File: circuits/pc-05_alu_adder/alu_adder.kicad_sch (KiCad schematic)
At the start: 10 parts, among them J1 Conn_01x10, U1 74LS83, U2 74LS83, U3 74AHC244

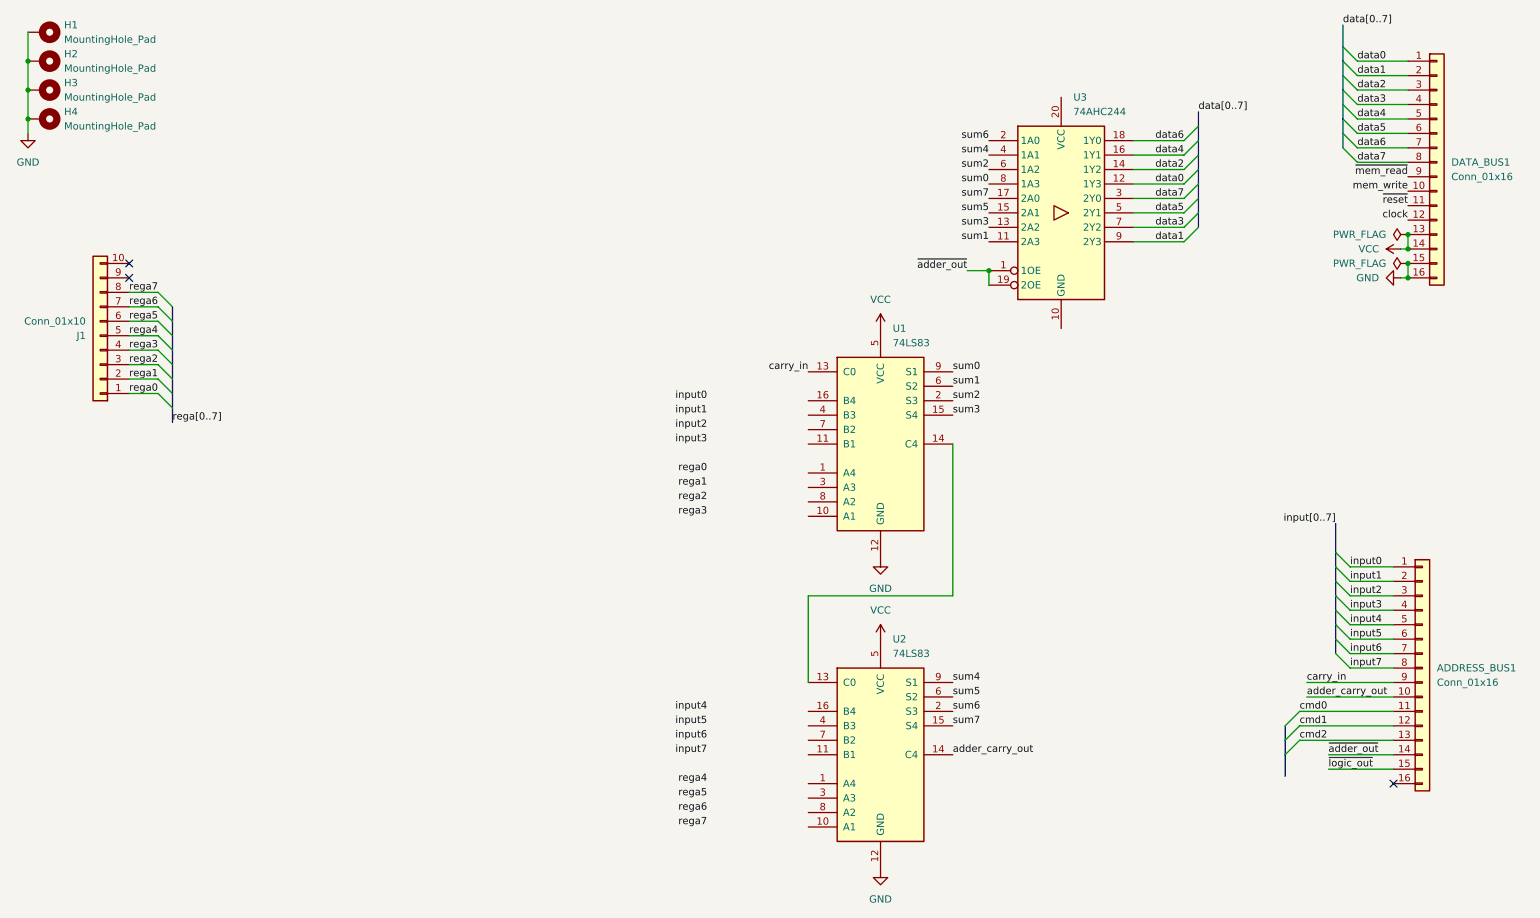
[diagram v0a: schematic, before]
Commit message: pc-05: ALU adder prototype
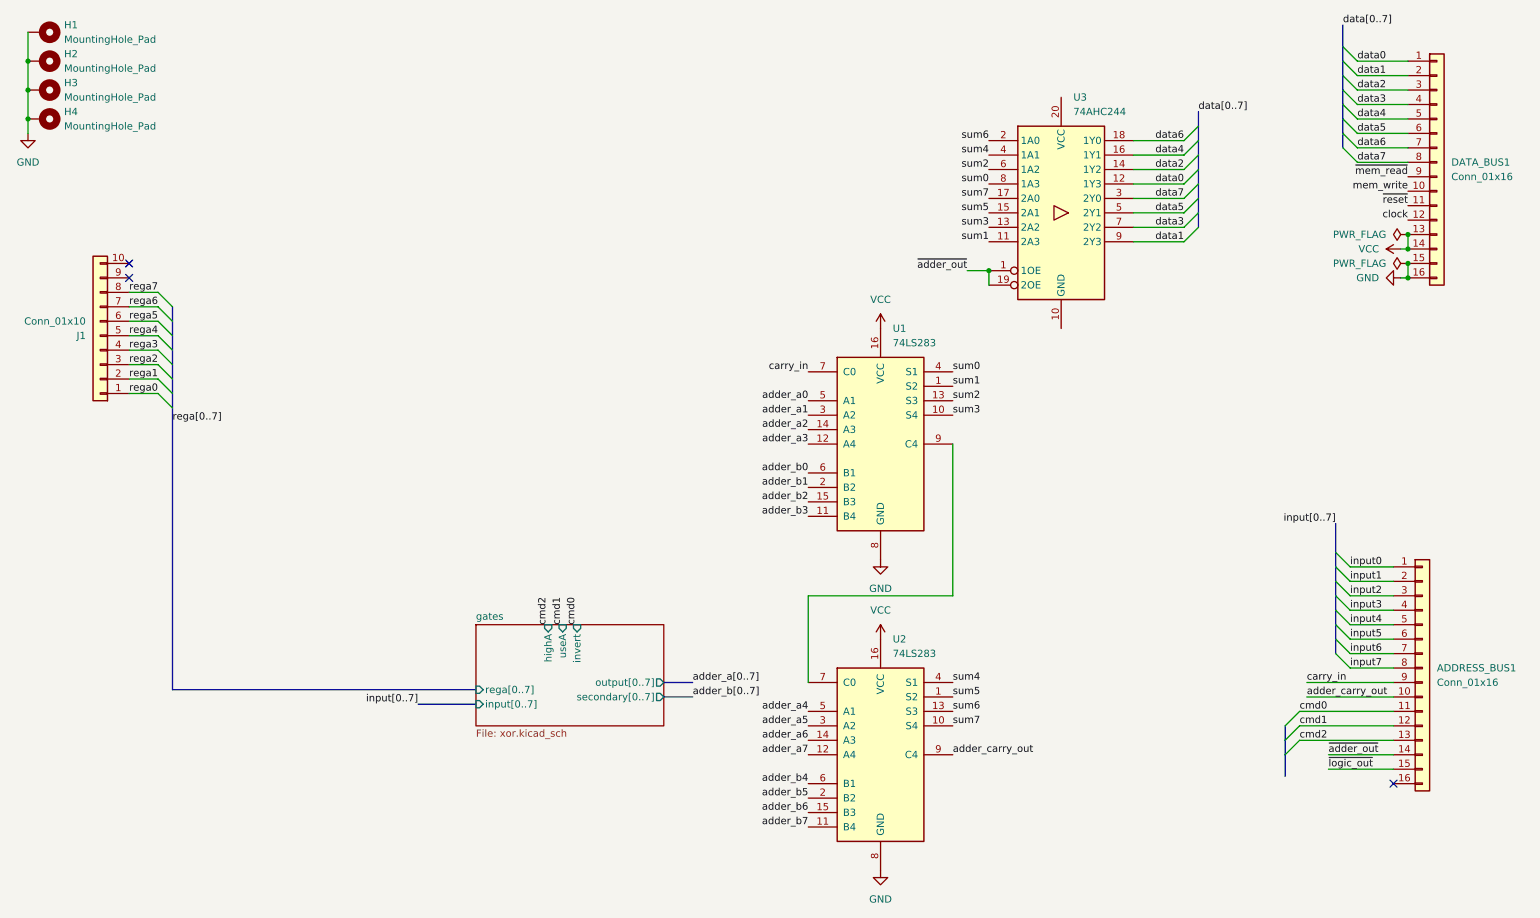
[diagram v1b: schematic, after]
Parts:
- removed U1, U2: 74LS83, Package_DIP:DIP-16_W7.62mm_LongPads, symbol 74xx:74LS83
- added U1, U2: 74LS283, Package_DIP:DIP-16_W7.62mm_LongPads, symbol 74xx:74LS283
- U3: footprint (none) -> Package_DIP:DIP-20_W7.62mm_LongPads
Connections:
- net GND: now also U1.8 (GND), U2.8 (GND)
- net VCC: now also U1.16 (VCC), U2.16 (VCC)
- net adder_carry_out: now also U2.9 (C4)
- net carry_in: now also U1.7 (C0)
- net sum0: now also U1.4 (S1)
- net sum1: now also U1.1 (S2)
- net sum2: now also U1.13 (S3)
- net sum3: now also U1.10 (S4)
- net sum4: now also U2.4 (S1)
- net sum5: now also U2.1 (S2)
- net sum6: now also U2.13 (S3)
- net sum7: now also U2.10 (S4)
- new net: U1.9 (C4), U2.7 (C0)
- new net adder_a0: U1.5 (A1)
- new net adder_a1: U1.3 (A2)
- new net adder_a2: U1.14 (A3)
- new net adder_a3: U1.12 (A4)
- new net adder_a4: U2.5 (A1)
- new net adder_a5: U2.3 (A2)
- new net adder_a6: U2.14 (A3)
- new net adder_a7: U2.12 (A4)
- new net adder_b0: U1.6 (B1)
- new net adder_b1: U1.2 (B2)
- new net adder_b2: U1.15 (B3)
- new net adder_b3: U1.11 (B4)
- new net adder_b4: U2.6 (B1)
- new net adder_b5: U2.2 (B2)
- new net adder_b6: U2.15 (B3)
- new net adder_b7: U2.11 (B4)
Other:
- added sheet gates (xor.kicad_sch)

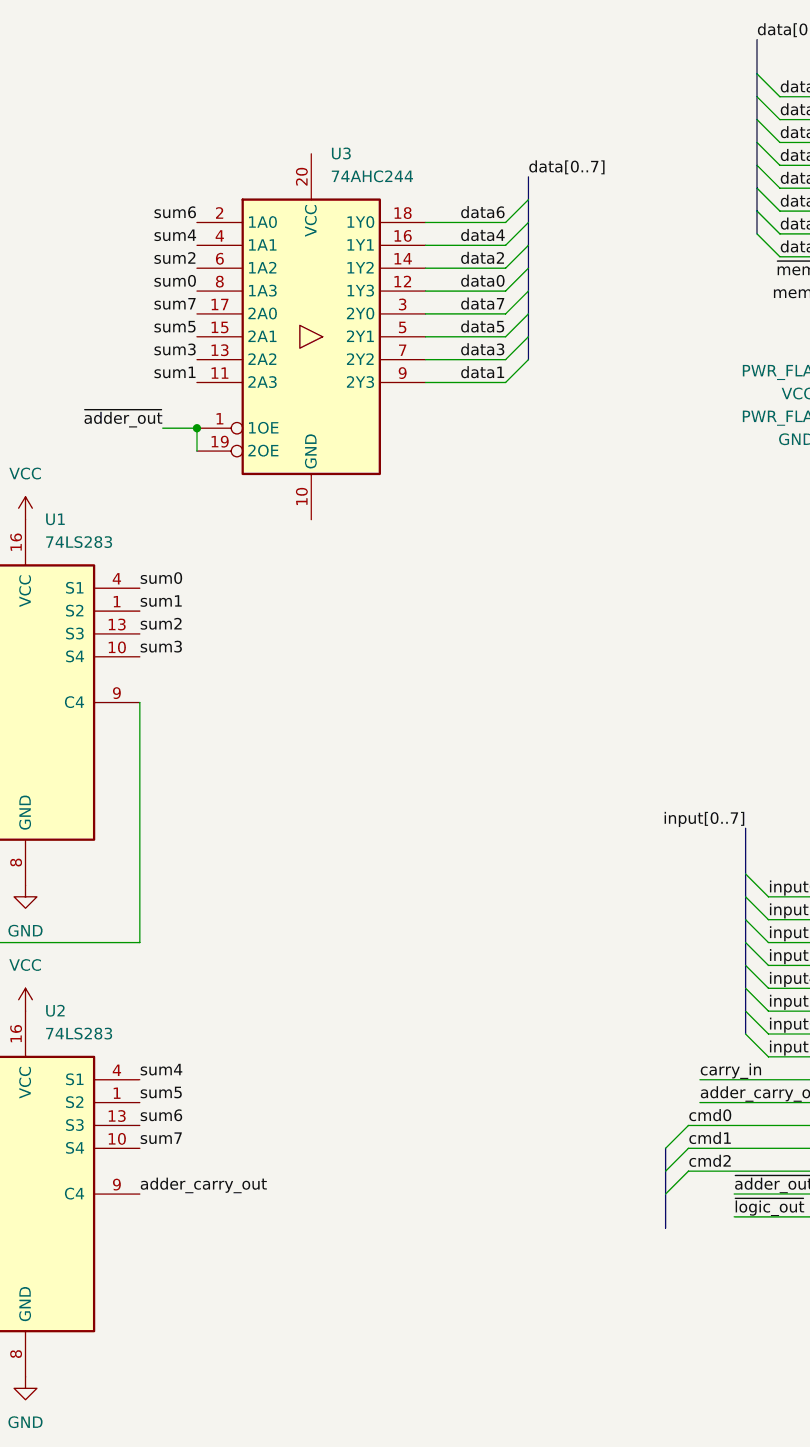
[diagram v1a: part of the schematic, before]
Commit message: pc-05: polishing of adder circuit
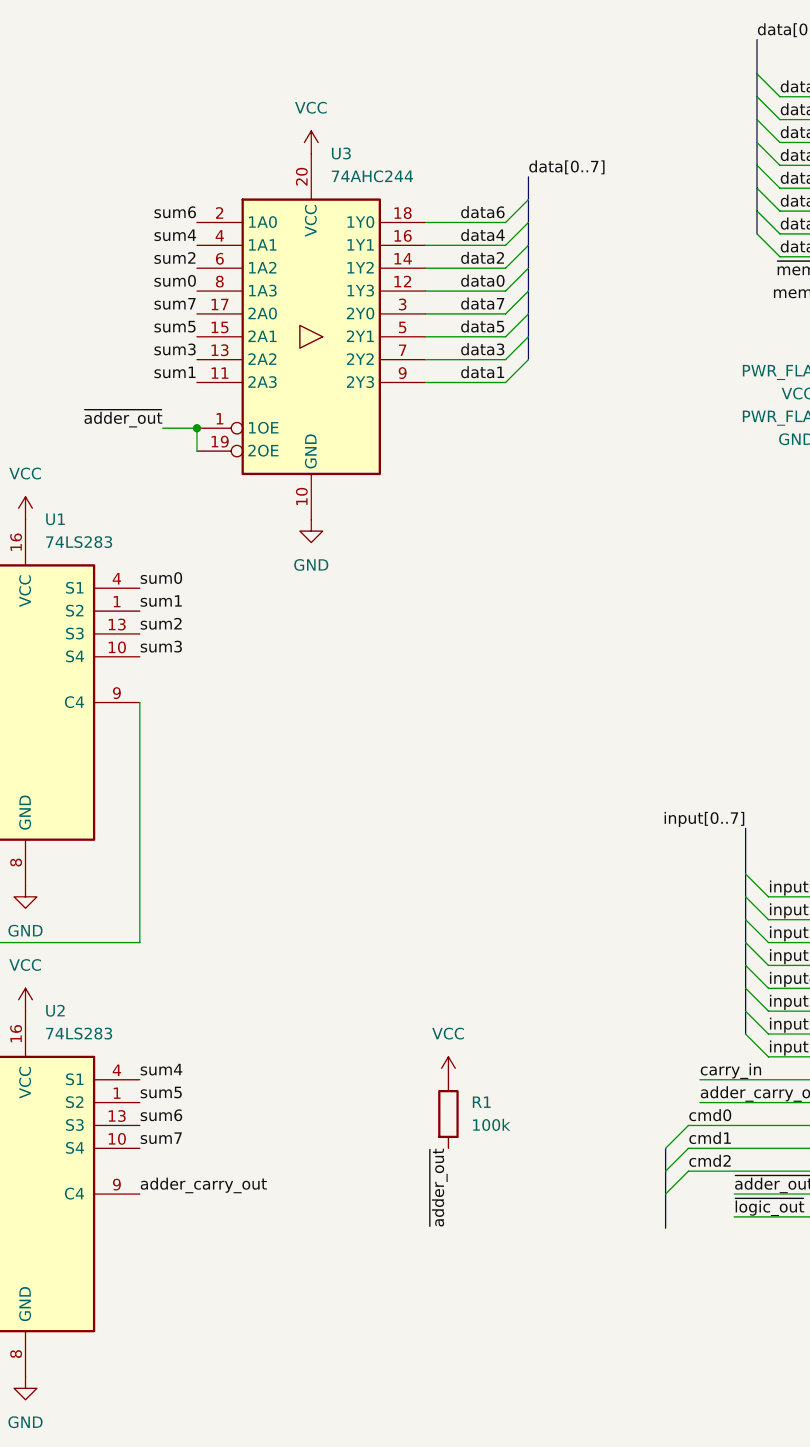
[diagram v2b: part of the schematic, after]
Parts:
- added R1: 100k, Resistor_SMD:R_0603_1608Metric, symbol Device:R
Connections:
- net GND: now also U3.10 (GND)
- net VCC: now also U3.20 (VCC), R1.1
- net ~{adder_out}: now also R1.2

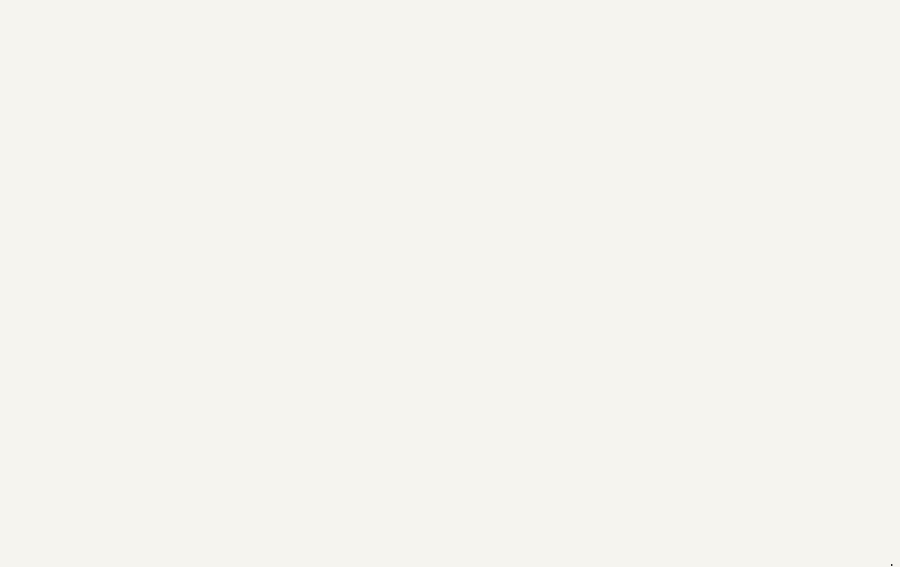
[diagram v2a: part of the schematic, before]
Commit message: add filter and decoupling capacitors to all boards
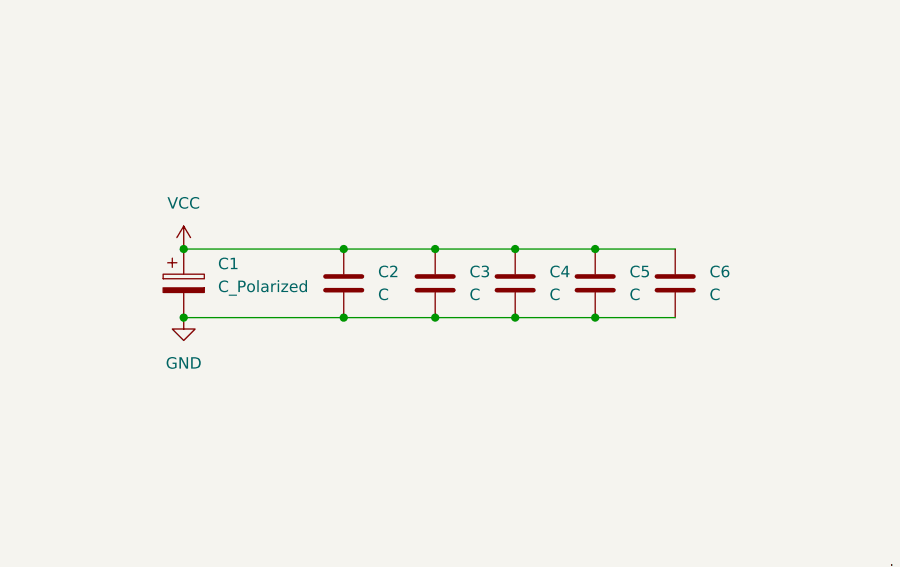
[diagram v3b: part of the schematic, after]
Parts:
- added C1: C_Polarized, Capacitor_SMD:CP_Elec_5x5.3, symbol Device:C_Polarized
- added C2, C3, C4, C5, C6: C, Capacitor_SMD:C_0603_1608Metric, symbol Device:C
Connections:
- net GND: now also C1.2, C2.2, C3.2, C4.2, C5.2, C6.2
- net VCC: now also C1.1, C2.1, C3.1, C4.1, C5.1, C6.1
